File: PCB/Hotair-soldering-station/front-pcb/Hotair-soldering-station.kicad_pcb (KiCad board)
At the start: 2 copper layers, 54 parts, among them J1 fan_reg_pot, J2 main-board-conn, J3 hot_on, J4 solder_on, Q1 BC817, Q10 BC807, Q11 BC807, Q12 BC807, Q13 BC807, Q14 BC807, Q2 BC817, Q3 BC817, Q4 BC817, Q5 BC817, Q6 BC817, Q7 BC817, Q8 BC817, Q9 BC807, SW1 SW_Push, SW2 SW_Push, SW3 SW_Push, SW4 SW_Push, U1 74HC595D, U2 74HC595D, U3 My-Footprints:3-digit-7-segme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

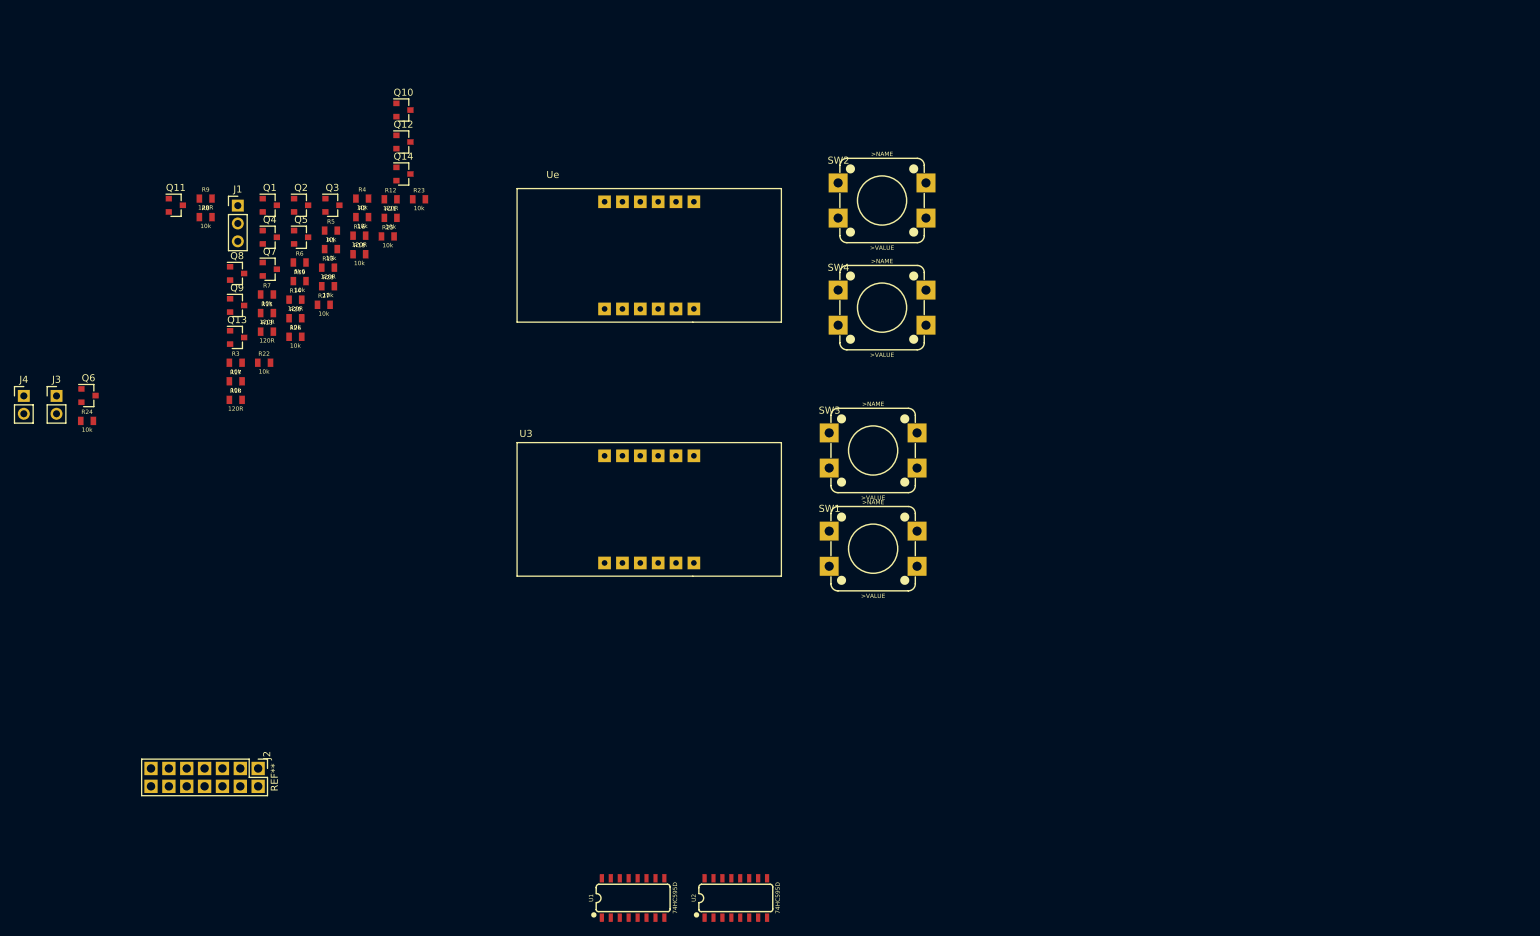
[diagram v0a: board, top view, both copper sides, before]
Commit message: main schematic update, front pcb routing
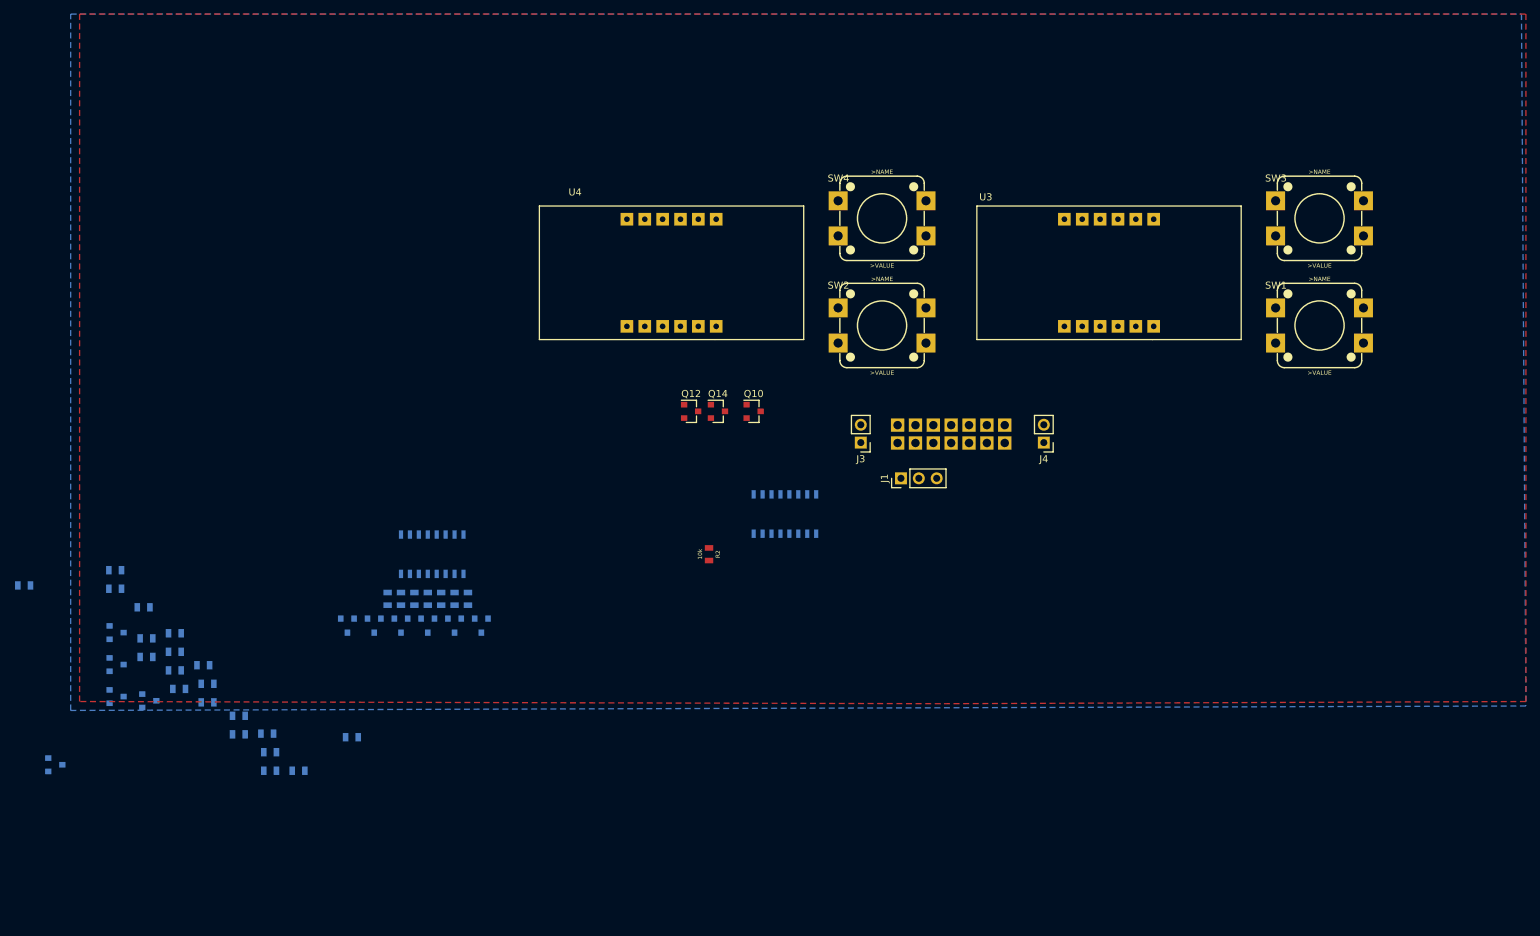
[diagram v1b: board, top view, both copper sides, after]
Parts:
- J2, Q1, Q11, Q13, Q2, Q3, Q4, Q5, Q6, Q7, Q8, Q9, R1, R10, R11, R12, R13, R14, R15, R16, R17, R18, R19, R20, R21, R22, R23, R24, R25, R26, R27, R28, R3, R4, R5, R6, R7, R8, R9, U1, U2: moved to B.Cu
- SW1: value SW_Push -> HOTAIR_UP
- SW2: value SW_Push -> HOTAIR_DOWN
- SW3: value SW_Push -> SIRON_UP
- SW4: value SW_Push -> SIRON_DOWN
- moved J4 145.2 mm to (156.2, 73.7), turned to 180 degrees
- moved J3 114.6 mm to (130.2, 73.7), turned to 180 degrees
- moved J2 114.4 mm to (152.4, 75.6), turned to 90 degrees
- moved J1 102.0 mm to (135.9, 78.7), turned to 90 degrees
- moved R12 83.1 mm to (46.2, 120.3)
- moved R23 83.1 mm to (50.2, 120.3)
- moved Q11 81.4 mm to (15.6, 119.5)
- moved R9 79.4 mm to (57.8, 115.6)
- moved R21 77.9 mm to (46.2, 117.7)
- moved U3 73.6 mm to (146.7, 40.0)
- moved R16 73.0 mm to (41.7, 115.2)
- moved R25 72.8 mm to (45.7, 115.1)
- moved SW3 71.6 mm to (189.2, 35.6)
- moved SW1 71.0 mm to (189.2, 50.8)
- moved R2 68.8 mm to (108.6, 89.5), turned to 270 degrees
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- renumbered Ue to U4
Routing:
- added copper zone on B.Cu, net GND
- added copper zone on F.Cu, net GND

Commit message: routing progress
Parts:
- Q10, Q12, Q14, R2: moved to B.Cu
- moved Q7 186.3 mm to (200.8, 38.4), turned to 180 degrees
- moved Q8 185.3 mm to (196.5, 41.3), turned to 180 degrees
- moved R15 182.7 mm to (206.3, 41.3), turned to 180 degrees
- moved R16 171.0 mm to (198.8, 47.5), turned to 180 degrees
- moved R27 166.8 mm to (200.7, 74.9), turned to 90 degrees
- moved Q11 164.9 mm to (173.1, 70.6), turned to 180 degrees
- moved R28 163.2 mm to (197.0, 74.4)
- moved R22 161.9 mm to (178.6, 37.2)
- moved R20 159.5 mm to (178.6, 39.1)
- moved R17 155.4 mm to (177.7, 71.0)
- moved Q9 154.5 mm to (173.0, 63.0), turned to 180 degrees
- moved R13 153.2 mm to (170.2, 43.1), turned to 180 degrees
- moved R14 153.1 mm to (170.3, 39.2), turned to 180 degrees
- moved R11 151.5 mm to (170.3, 50.7), turned to 180 degrees
- moved R10 151.0 mm to (170.4, 54.5), turned to 180 degrees
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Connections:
- net Net-(R17-Pad2) renamed IRON_DIG2
- net Net-(R19-Pad2) renamed HOTAIR_DIG2
- R1 pad 1: Net-(R1-Pad1) -> SEG_DP
- R18 pad 2: Net-(R18-Pad2) -> IRON_DIG3
- R2 pad 1: Net-(R2-Pad1) -> SEG_G
- R20 pad 2: Net-(R20-Pad2) -> HOTAIR_DIG3
- R21 pad 2: Net-(R21-Pad2) -> IRON_DIG1
- R22 pad 2: Net-(R22-Pad2) -> HOTAIR_DIG1
- R3 pad 1: Net-(R3-Pad1) -> SEG_F
- R4 pad 1: Net-(R4-Pad1) -> SEG_E
- R5 pad 1: Net-(R5-Pad1) -> SEG_D
- R6 pad 1: Net-(R6-Pad1) -> SEG_C
- R7 pad 1: Net-(R7-Pad1) -> SEG_B
- R8 pad 1: Net-(R8-Pad1) -> SEG_A
- U1 pad 1: Net-(R2-Pad1) -> SEG_B
- U1 pad 15: Net-(R1-Pad1) -> SEG_A
- U1 pad 2: Net-(R3-Pad1) -> SEG_C
- U1 pad 3: Net-(R4-Pad1) -> SEG_D
- U1 pad 4: Net-(R5-Pad1) -> SEG_E
- U1 pad 5: Net-(R6-Pad1) -> SEG_F
- U1 pad 6: Net-(R7-Pad1) -> HOTAIR_DIG3
- U1 pad 7: Net-(R8-Pad1) -> HOTAIR_DIG1
- U2 pad 15: Net-(R20-Pad2) -> SEG_DP
- U2 pad 2: Net-(R22-Pad2) -> SEG_G
- U2 pad 3: Net-(R18-Pad2) -> IRON_DIG1
- U2 pad 5: Net-(R21-Pad2) -> IRON_DIG3
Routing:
- net Net-(Q12-Pad3): track 0.00 -> 54.7 mm
- net Net-(R10-Pad2): track 0.00 -> 51.9 mm
- net Net-(R14-Pad2): track 0.00 -> 51.8 mm
- net Net-(R9-Pad2): track 0.00 -> 48.5 mm
- net Net-(R13-Pad2): track 0.00 -> 45.8 mm
- net Net-(R12-Pad2): track 0.00 -> 41.8 mm
- net Net-(R11-Pad2): track 0.00 -> 39.7 mm
- net Net-(R16-Pad2): track 0.00 -> 38.9 mm
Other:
- board outline added: 120 x 70 mm
- net class Default: clearance 0.2 -> 0.5
- rule trace_clearance: 0.2 -> 0.5

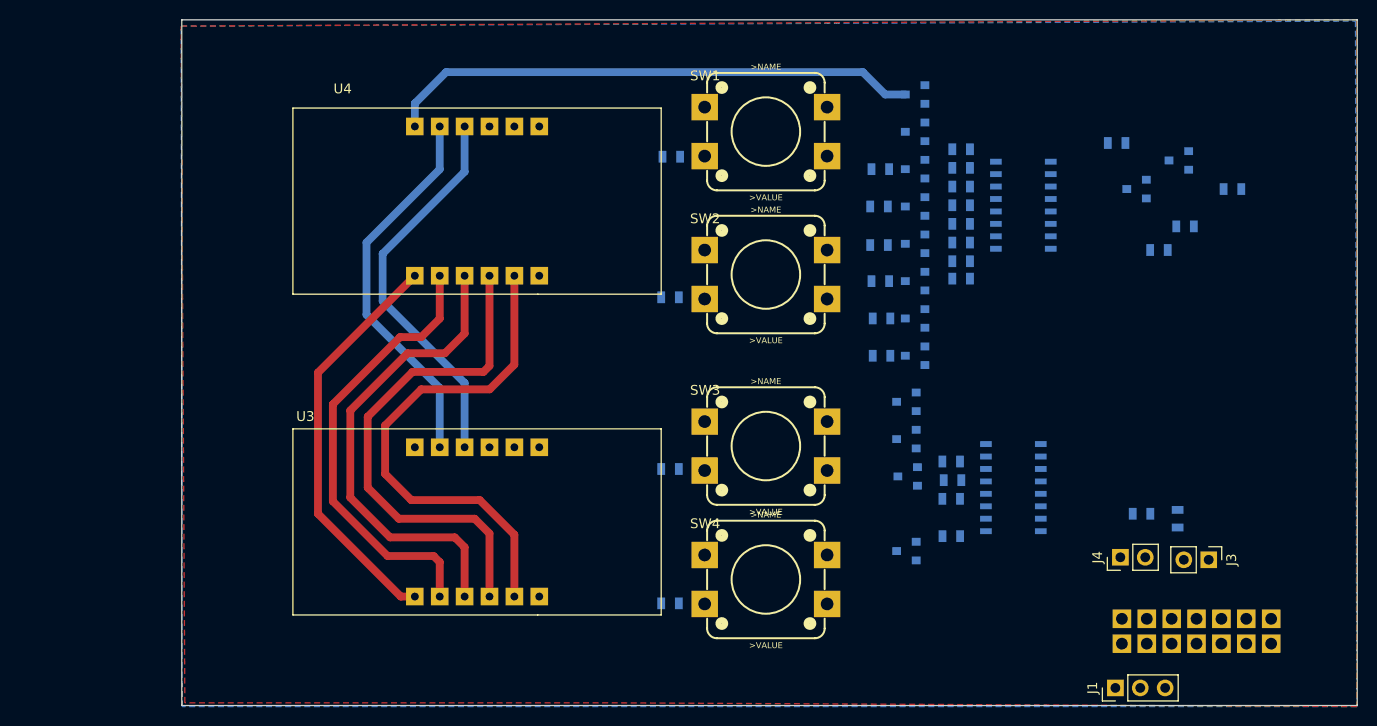
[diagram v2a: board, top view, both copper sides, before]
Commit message: add hot air fan buttons
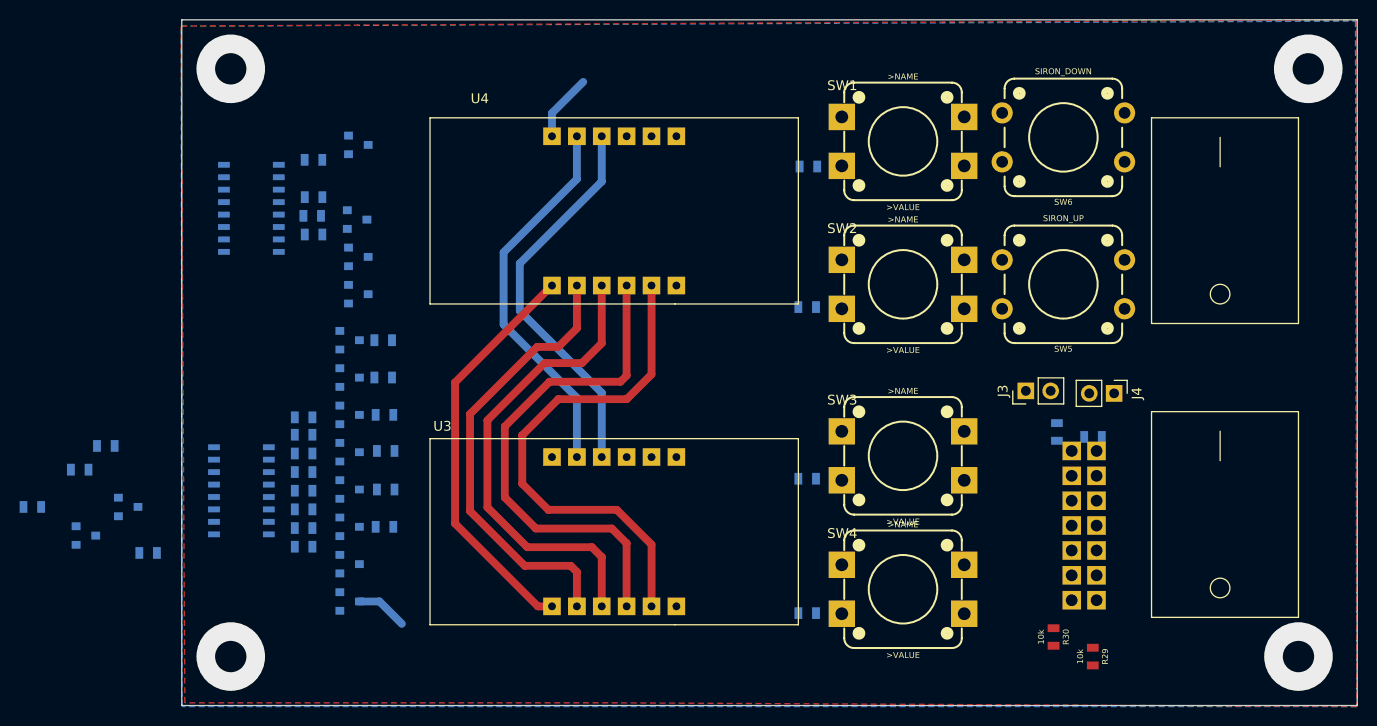
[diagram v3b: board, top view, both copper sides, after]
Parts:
- removed J1: fan_reg_pot, Connector_PinHeader_2.54mm:PinHeader_1x03_P2.54mm_Vertical
- added R29: 10k, Capacitors:0805, F.Cu at (192.0, 89.0)
- added R30: 10k, Capacitors:0805, F.Cu at (188.0, 87.0)
- added SW5: SIRON_UP, Switches:TACTILE_SWITCH_PTH_12MM, F.Cu at (189.0, 51.0)
- added SW6: SIRON_DOWN, Switches:TACTILE_SWITCH_PTH_12MM, F.Cu at (189.0, 36.0)
- moved R15 126.7 mm to (83.7, 73.7), turned to 0 degrees
- moved Q7 118.0 mm to (89.2, 76.6), turned to 0 degrees
- moved R8 115.5 mm to (88.6, 69.9), turned to 0 degrees
- moved R16 109.4 mm to (91.2, 67.5), turned to 0 degrees
- moved Q8 107.9 mm to (93.5, 73.7), turned to 0 degrees
- moved R7 107.4 mm to (95.6, 78.4), turned to 0 degrees
- moved U1 85.0 mm to (105.1, 72.1), turned to 270 degrees
- moved U2 82.9 mm to (106.1, 43.2), turned to 270 degrees
- moved R22 78.4 mm to (111.4, 77.8), turned to 180 degrees
- moved Q12 77.5 mm to (116.1, 83.4), turned to 0 degrees
- moved R20 76.5 mm to (111.4, 75.9), turned to 180 degrees
- moved R19 75.6 mm to (112.4, 38.3), turned to 180 degrees
- moved R6 74.8 mm to (111.4, 74.0), turned to 0 degrees
- moved R5 73.2 mm to (111.4, 72.1), turned to 0 degrees
- moved Q14 72.7 mm to (116.1, 79.6), turned to 0 degrees
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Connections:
- J2 pad 5: Net-(J1-Pad3) -> HOTAIR_FAN_DOWN_SW
- J2 pad 6: Net-(J1-Pad2) -> HOTAIR_FAN_UP_SW
- J2 pad 7: Net-(J1-Pad1) -> GND
- U1 pad 5: SEG_F -> HOTAIR_DIG3
- U1 pad 6: HOTAIR_DIG3 -> HOTAIR_DIG2
- U2 pad 1: HOTAIR_DIG2 -> SEG_F
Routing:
- net Net-(Q12-Pad3): track 54.7 -> 12.1 mm
- net (no net): vias 0 -> 4

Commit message: front PCB - finish
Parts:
- added C1: 100n, Capacitors:0805, B.Cu at (106.0, 66.9)
- added C2: 100n, Capacitors:0805, B.Cu at (104.2, 37.0)
- added C3: 47u, Capacitor_Tantalum_SMD:CP_EIA-3528-21_Kemet-B, B.Cu at (107.4, 59.7)
- R27, R28: moved to F.Cu
- R29, R30: moved to B.Cu
- SW1, SW2, SW3, SW4: footprint My-Footprints:push_button_12mm -> Switches:TACTILE_SWITCH_PTH_12MM
- moved R15 58.0 mm to (121.3, 29.5)
- moved Q7 55.2 mm to (117.9, 29.5)
- moved R30 53.8 mm to (192.1, 33.3), turned to 180 degrees
- moved R7 51.7 mm to (114.6, 30.4)
- moved Q14 46.0 mm to (117.9, 33.6)
- moved Q12 41.9 mm to (117.9, 41.5)
- moved R20 41.5 mm to (114.6, 34.5)
- moved R29 40.3 mm to (192.2, 48.7), turned to 180 degrees
- moved R22 35.4 mm to (114.5, 42.5)
- moved R21 33.6 mm to (115.8, 79.4)
- moved R16 31.9 mm to (122.3, 74.7)
- moved U2 30.5 mm to (107.8, 73.7)
- moved J4 29.8 mm to (205.4, 89.7)
- moved U1 28.6 mm to (105.5, 43.4)
- moved R8 27.9 mm to (115.8, 75.7)
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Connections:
- J2 pad 11: SOLDER_DOWN_SW -> SOLDER_ON_SW
- J2 pad 12: SOLDER_UP_SW -> 7SEG_CLK
- J2 pad 13: HOTAIR_DOWN_SW -> 7SEG_LATCH
- J2 pad 14: HOTAIR_UP_SW -> 7SEG_DIN
- J2 pad 2: 7SEG_DIN -> GND
- J2 pad 3: 7SEG_CLK -> GND
- J2 pad 4: 7SEG_LATCH -> SOLDER_DOWN_SW
- J2 pad 5: HOTAIR_FAN_DOWN_SW -> SOLDER_UP_SW
- J2 pad 6: HOTAIR_FAN_UP_SW -> HOTAIR_DOWN_SW
- J2 pad 7: GND -> HOTAIR_UP_SW
- J2 pad 8: GND -> HOTAIR_FAN_UP_SW
- J2 pad 9: SOLDER_ON_SW -> HOTAIR_FAN_DOWN_SW
- U1 pad 1: SEG_B -> HOTAIR_DIG3
- U1 pad 15: SEG_A -> SEG_B
- U1 pad 2: SEG_C -> HOTAIR_DIG2
- U1 pad 3: SEG_D -> HOTAIR_DIG1
- U1 pad 4: SEG_E -> SEG_G
- U1 pad 5: HOTAIR_DIG3 -> SEG_C
- U1 pad 6: HOTAIR_DIG2 -> SEG_DP
- U1 pad 7: HOTAIR_DIG1 -> SEG_D
- U2 pad 1: SEG_F -> IRON_DIG2
- U2 pad 15: SEG_DP -> IRON_DIG3
- U2 pad 2: SEG_G -> SEG_F
- U2 pad 3: IRON_DIG1 -> SEG_A
- U2 pad 4: IRON_DIG2 -> IRON_DIG1
- U2 pad 5: IRON_DIG3 -> SEG_E
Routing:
- net +3V3: track 0.00 -> 322.1 mm, vias 0 -> 8
- net 7SEG_CLK: track 0.00 -> 156.2 mm
- net 7SEG_LATCH: track 0.00 -> 145.1 mm, vias 0 -> 2
- net 7SEG_DIN: track 0.00 -> 143.0 mm, vias 0 -> 1
- net Net-(R15-Pad2): track 0.06 -> 68.9 mm
- net HOTAIR_FAN_DOWN_SW: track 0.00 -> 56.1 mm
- net HOTAIR_UP_SW: track 0.00 -> 49.9 mm
- net HOTAIR_DOWN_SW: track 0.00 -> 42.8 mm
- net Net-(Q11-Pad3): track 0.00 -> 34.8 mm
- net SOLDER_DOWN_SW: track 0.00 -> 33.5 mm
- net SOLDER_UP_SW: track 0.00 -> 33.1 mm
- net Net-(Q10-Pad3): track 0.00 -> 32.4 mm
- net Net-(Q14-Pad3): track 0.00 -> 32.1 mm
- net HOTAIR_ON_SW: track 0.00 -> 31.4 mm
- net Net-(R13-Pad2): track 45.8 -> 76.2 mm
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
